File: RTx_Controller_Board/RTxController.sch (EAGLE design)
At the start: 91 parts, among them IC1 LTC4263, IC2 TLK110", U2 TPD4S012, X4 MINI-USB-32005-301

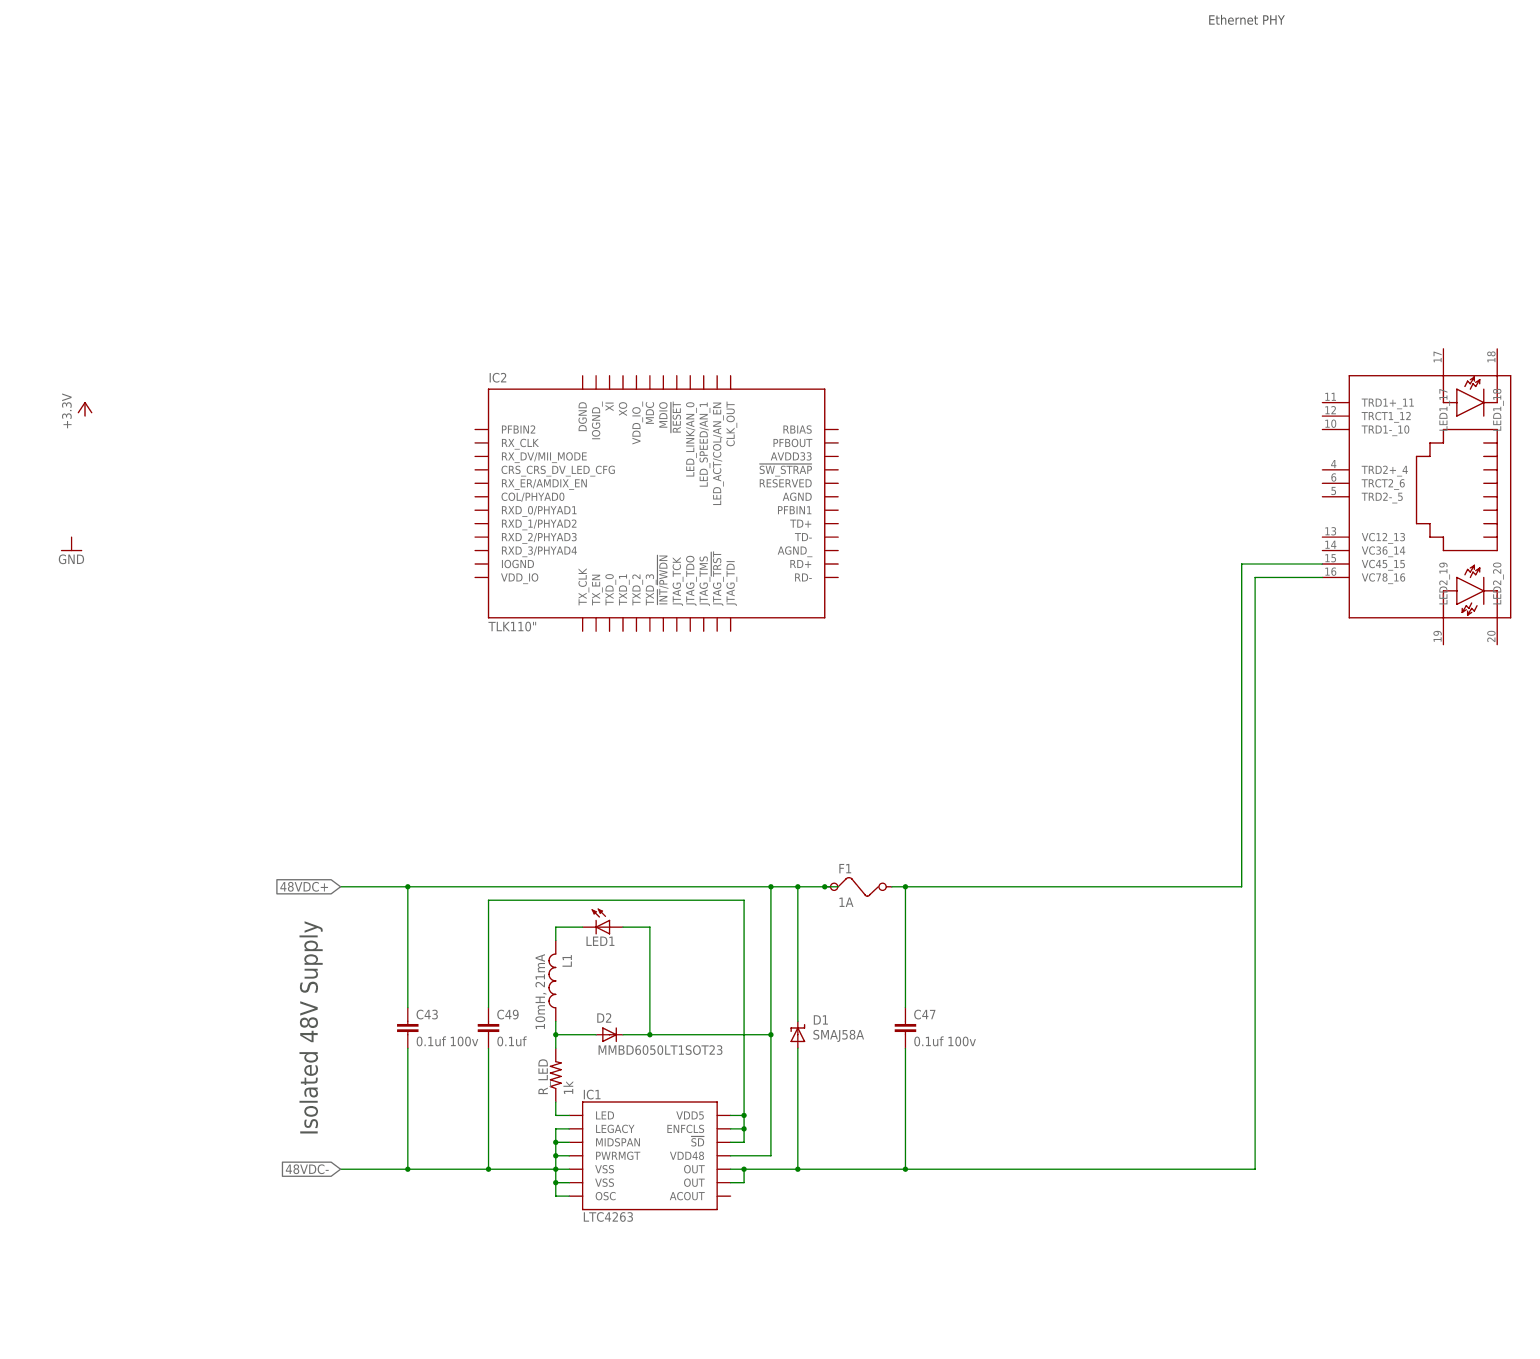
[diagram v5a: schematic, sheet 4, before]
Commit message: Updated Ethernet PHY components and schematic.
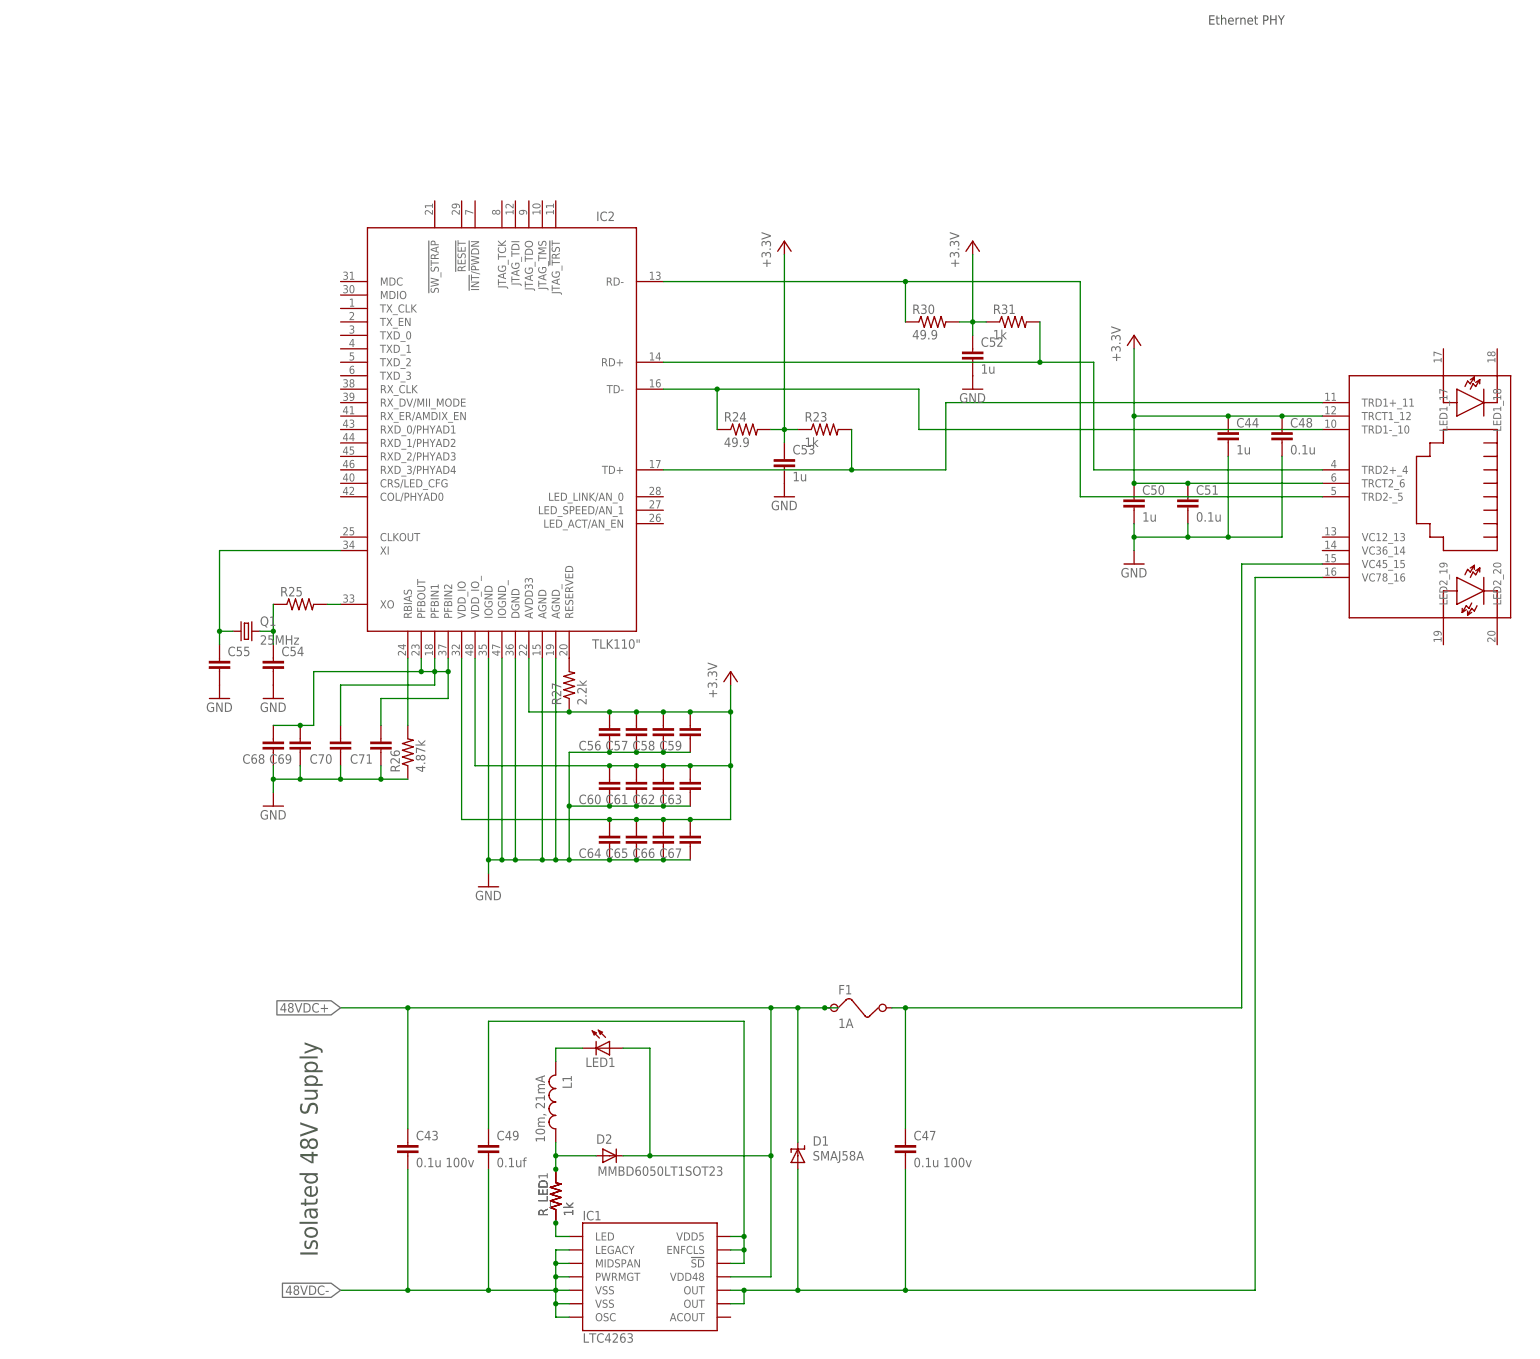
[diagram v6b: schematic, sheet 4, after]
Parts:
- added C44, C50, C52, C53: 1u, motorFeedback:C-EUC0805K
- added C48, C51: 0.1u, motorFeedback:C-EUC0805K
- added C54, C55, C56, C57, C58, C59, C60, C61, C62, C63, C64, C65, C66, C67, C68, C69, C70, C71: (no value), motorFeedback:C-EUC0805K
- added Q1: 25MHz, motorFeedback:CRYTAL
- added R23, R31, R_LED1: 1k, motorFeedback:R-US_R0603
- added R24, R30: 49.9, motorFeedback:R-US_R0603
- added R25: (no value), motorFeedback:R-US_R0603
- added R26: 4.87k, motorFeedback:R-US_R0603
- added R27: 2.2k, motorFeedback:R-US_R0603
- C43, C47: value 0.1uf 100v -> 0.1u 100v
- L1: value 10mH, 21mA -> 10m, 21mA
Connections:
- new net N$26: IC2.TD+, R23.2, U$6.TRD1+_11
- new net N$27: IC2.TD-, R24.1, U$6.TRD1-_10
- new net N$28: IC2.RD+, R31.2, U$6.TRD2+_4
- new net N$29: IC2.RD-, R30.1, U$6.TRD2-_5
- new net N$30: C53.1, R23.1, R24.2
- new net N$31: IC2.XO, R25.2
- new net N$32: C55.1, IC2.XI, Q1.1
- new net N$33: C54.1, Q1.2, R25.1
- new net N$34: IC2.RESERVED, R27.2
- new net N$40: IC2.RBIAS, R26.2
- new net N$41: C68.2, C69.2, C70.2, C71.2, IC2.PFBIN1, IC2.PFBIN2, IC2.PFBOUT
- net +3.3V: now also C44.1, C48.1, C50.1, C51.1, C52.1, C56.2, C57.2, C58.2, C59.2, C60.2, C61.2, C62.2, C63.2, C64.2, C65.2, C66.2, C67.2, IC2.AVDD33, IC2.VDD_IO, IC2.VDD_IO_, R27.1, R30.2, R31.1, U$6.TRCT1_12, U$6.TRCT2_6
- net GND: now also C44.2, C48.2, C50.2, C51.2, C52.2, C53.2, C54.2, C55.2, C56.1, C57.1, C58.1, C59.1, C60.1, C61.1, C62.1, C63.1, C64.1, C65.1, C66.1, C67.1, C68.1, C69.1, C70.1, C71.1, IC2.AGND, IC2.AGND_, IC2.DGND, IC2.IOGND, IC2.IOGND_, R26.1
- net N$24: now also R_LED1.2
- net N$25: now also R_LED1.1
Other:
- moved on the sheet: C43, C47, C49, D1, D2, F1, IC1, L1, LED1, R_LED

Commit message: Added Ethernet pinouts to MCU.
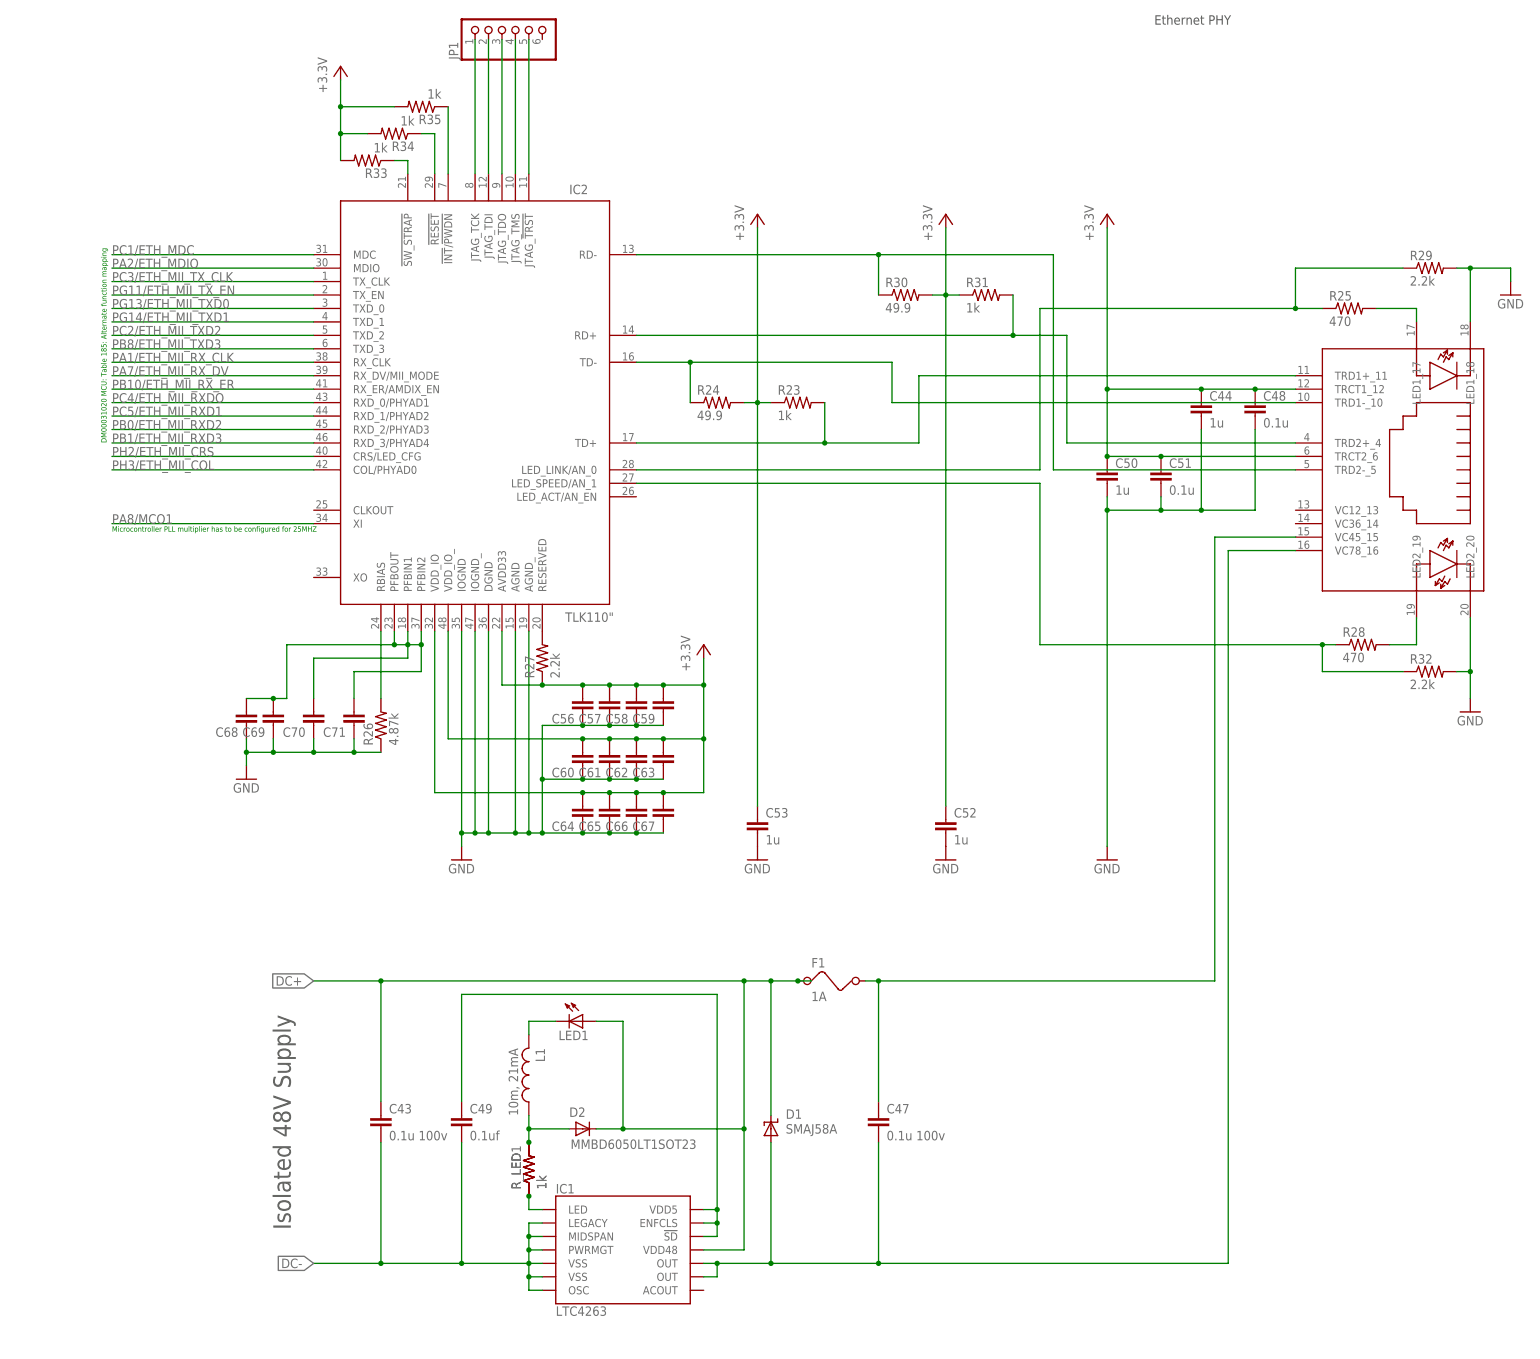
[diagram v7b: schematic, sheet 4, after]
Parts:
- removed C54, C55: (no value), motorFeedback:C-EUC0805K
- removed Q1: 25MHz, motorFeedback:CRYTAL
- added JP1: (no value), motorFeedback:PINHD-1X6
- added R28: 470, motorFeedback:R-US_R0603
- added R29, R32: 2.2k, motorFeedback:R-US_R0603
- added R33, R34, R35: 1k, motorFeedback:R-US_R0603
- R25: value (none) -> 470
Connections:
- net 48VDC+ renamed DC+
- net 48VDC- renamed DC-
- new net N$35: R25.2, U$6.LED1_17
- new net N$36: IC2.LED_SPEED/AN_1, R28.1, R32.1
- new net N$37: IC2.!RESET!, R34.1
- new net N$38: IC2.!INT!/!PWDN!, R35.1
- new net N$56: IC2.JTAG_TCK, JP1.1
- new net N$57: IC2.JTAG_TDI, JP1.2
- new net N$58: IC2.JTAG_TDO, JP1.3
- new net N$59: IC2.JTAG_TMS, JP1.4
- new net N$60: IC2.JTAG_!TRST!, JP1.5
- new net PA1/ETH_MII_RX_CLK: IC2.RX_CLK
- new net PA2/ETH_MDIO: IC2.MDIO
- new net PA7/ETH_MII_RX_DV: IC2.RX_DV/MII_MODE
- new net PA8/MCO1: IC2.XI
- new net PB0/ETH_MII_RXD2: IC2.RXD_2/PHYAD3
- new net PB1/ETH_MII_RXD3: IC2.RXD_3/PHYAD4
- new net PB10/ETH_MII_RX_ER: IC2.RX_ER/AMDIX_EN
- new net PB8/ETH_MII_TXD3: IC2.TXD_3
- new net PC1/ETH_MDC: IC2.MDC
- new net PC2/ETH_MII_TXD2: IC2.TXD_2
- new net PC3/ETH_MII_TX_CLK: IC2.TX_CLK
- new net PC4/ETH_MII_RXDO: IC2.RXD_0/PHYAD1
- new net PC5/ETH_MII_RXD1: IC2.RXD_1/PHYAD2
- new net PG11/ETH_MII_TX_EN: IC2.TX_EN
- new net PG13/ETH_MII_TXD0: IC2.TXD_0
- new net PG14/ETH_MII_TXD1: IC2.TXD_1
- new net PH2/ETH_MII_CRS: IC2.CRS/LED_CFG
- new net PH3/ETH_MII_COL: IC2.COL/PHYAD0
- net +3.3V: now also R33.2, R34.2, R35.2
- net GND: now also R29.2, R32.2, U$6.LED1_18, U$6.LED2_20; no longer C54.2, C55.2
- net N$31: now also IC2.!SW_STRAP!, R33.1; no longer IC2.XO, R25.2
- net N$32: now also R28.2, U$6.LED2_19; no longer C55.1, IC2.XI, Q1.1
- net N$33: now also IC2.LED_LINK/AN_0, R29.1; no longer C54.1, Q1.2
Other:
- note added: "DM00031020 MCU: Table 185: Alternate function mapping"
- note added: "Microcontroller PLL multiplier has to be configured for 25MHZ"
- moved on the sheet: C43, C44, C47, C48, C49, C50, C51, C52, C53, C56, C57, C58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

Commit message: Added CPU to schematic, completed pin-out of GMD signals, Ethernet signals, USB signals. Needs JTAG connector, ESD protection.
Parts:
- added C100, C101, C102, C103, C104, C105, C106, C107, C108, C109, C110, C111, C112, C113, C114, C115, C116, C117, C118, C119, C120, C121, C122, C123, C124, C93, C94, C95, C96, C97, C98, C99: (no value), motorFeedback:C-EUC0603
- added C54, C55, C72, C73, C74, C75, C76, C77, C78, C79, C80, C81, C82, C83, C84, C88, C90, C92: 0.1u, motorFeedback:C-EUC0402
- added C85: 4.7u, motorFeedback:C-EUC0603
- added C86, C87: 2.2u, motorFeedback:C-EUC0402
- added C89, C91: 1.0u, motorFeedback:C-EUC0402
- added R36: 0, motorFeedback:R-US_R0603
- added R37, R39, R40, R41, R42, R43, R44, R45, R46, R47, R48, R49, R50, R51, R52, R53: (no value), motorFeedback:R-US_R0603
- added R38: 10k, motorFeedback:R-US_R0603
- added SW1: COM08720, motorFeedback:COM08720
- added U1: STM32F407ZXT, motorFeedback:STM32F407ZXT
- added X3: (no value), con-subd:F15HDHS
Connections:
- removed net CNV: ADC1.CNV@6, ADC1.SDI@9, ADC2.CNV@6, ADC3.CNV@6, ADC4.CNV@6
- removed net PA1/ETH_MII_RX_CLK: IC2.RX_CLK
- removed net PA10/ID: U2.ID, X4.4
- removed net PA11/D-: R21.2
- removed net PA12/D+: R22.2
- removed net PA2/ETH_MDIO: IC2.MDIO
- removed net PA7/ETH_MII_RX_DV: IC2.RX_DV/MII_MODE
- removed net PA8/MCO1: IC2.XI
- removed net PA9/BBUS: C45.1, C46.1, U2.VBUS, X4.1
- removed net PB0/ETH_MII_RXD2: IC2.RXD_2/PHYAD3
- removed net PB1/ETH_MII_RXD3: IC2.RXD_3/PHYAD4
- removed net PB10/ETH_MII_RX_ER: IC2.RX_ER/AMDIX_EN
- removed net PB8/ETH_MII_TXD3: IC2.TXD_3
- removed net PC1/ETH_MDC: IC2.MDC
- removed net PC2/ETH_MII_TXD2: IC2.TXD_2
- removed net PC3/ETH_MII_TX_CLK: IC2.TX_CLK
- removed net PC4/ETH_MII_RXDO: IC2.RXD_0/PHYAD1
- removed net PC5/ETH_MII_RXD1: IC2.RXD_1/PHYAD2
- removed net PG11/ETH_MII_TX_EN: IC2.TX_EN
- removed net PG13/ETH_MII_TXD0: IC2.TXD_0
- removed net PG14/ETH_MII_TXD1: IC2.TXD_1
- removed net PH2/ETH_MII_CRS: IC2.CRS/LED_CFG
- removed net PH3/ETH_MII_COL: IC2.COL/PHYAD0
- removed net SCK: ADC1.SCK@8, ADC2.SCK@8, ADC3.SCK@8, ADC4.SCK@8
- removed net SDO: R16.2, R20.2
- new net ENABLE_AXIS3_OUT: C116.1, R46.2, U1-IO.PD0@81
- new net ENABLE_AXIS4_OUT: C114.1, R48.2, U1-IO.PD2@83
- new net ENABLE_LAT_OUT: C107.1, R43.2, U1-IO.PD11@58
- new net ENABLE_VERT_OUT: C105.1, R45.2, U1-IO.PD6@87
- new net ETH_MCO1: IC2.XI, U1-IO.PA8/MCO1@67
- new net ETH_MDC: IC2.MDC, U1-IO.PC1/ETH_MDC@16
- new net ETH_MDIO: IC2.MDIO, U1-IO.PA2/ETH_MDIO@25
- new net ETH_MII_COL: IC2.COL/PHYAD0, U1-IO.PA3/ETH_MII_COL@26
- new net ETH_MII_CRS: IC2.CRS/LED_CFG, U1-IO.PA0/ETH_MII_CRS@23
- new net ETH_MII_RXD0: IC2.RXD_0/PHYAD1, U1-IO.PC4/ETH_MII_RXD0@33
- new net ETH_MII_RXD1: IC2.RXD_1/PHYAD2, U1-IO.PC5/ETH_MII_RXD1@34
- new net ETH_MII_RXD2: IC2.RXD_2/PHYAD3, U1-IO.PB0/ETH_MII_RXD2@35
- new net ETH_MII_RXD3: IC2.RXD_3/PHYAD4, U1-IO.PB1/ETH_MII_RXD3@36
- new net ETH_MII_RX_CLK: IC2.RX_CLK, U1-IO.PA1/ETH_MII_RX_CLK@24
- new net ETH_MII_RX_DV: IC2.RX_DV/MII_MODE, U1-IO.PA7/ETH_MII_RX_DV@32
- new net ETH_MII_RX_ER: IC2.RX_ER/AMDIX_EN, U1-IO.PB10/ETH_MII_RX_ER@47
- new net ETH_MII_TXD0: IC2.TXD_0, U1-IO.PB12/ETH_MII_TXD0@51
- new net ETH_MII_TXD1: IC2.TXD_1, U1-IO.PB13/ETH_MII_TXD1@52
- new net ETH_MII_TXD2: IC2.TXD_2, U1-IO.PC2/ETH_MII_TXD2@17
- new net ETH_MII_TXD3: IC2.TXD_3, U1-IO.PB8/ETH_MII_TXD3@95
- new net ETH_MII_TX_CLK: IC2.TX_CLK, U1-IO.PC3/ETH_MII_TX_CLK@18
- new net ETH_MII_TX_EN: IC2.TX_EN, U1-IO.PB11/ETH_MII_TX_EN@48
- new net N$39: C92.1, SW1.1@1, SW1.3@3, U1-PWR.NRST@14
- new net N$42: C96.1, R37.1, X2-15.F
- new net N$43: R36.2, U1-PWR.VBAT@6
- new net N$44: R38.1, U1-PWR.BOOT0@94
- new net N$45: C95.1, R39.1, X2-14.F
- new net N$46: C94.1, R40.1, X2-13.F
- new net N$47: C93.1, R41.1, X2-12.F
- new net N$48: C104.1, R42.1, X2-4.F
- new net N$49: C103.1, R43.1, X2-3.F
- new net N$50: C102.1, R44.1, X2-2.F
- new net N$51: C101.1, R45.1, X2-1.F
- new net N$52: C112.1, R46.1, X3-4.F
- new net N$53: C111.1, R47.1, X3-3.F
- new net N$54: C110.1, R48.1, X3-2.F
- new net N$55: C109.1, R49.1, X3-1.F
- new net N$61: C120.1, R50.1, X3-15.F
- new net N$62: C119.1, R51.1, X3-14.F
- new net N$63: C118.1, R52.1, X3-13.F
- new net N$64: C117.1, R53.1, X3-12.F
- new net PWM_AXIS3_U_OUT: C123.1, R51.2, U1-IO.PC7@64
- new net PWM_AXIS3_V_OUT: C124.1, R50.2, U1-IO.PC6@63
- new net PWM_AXIS4_U_OUT: C121.1, R53.2, U1-IO.PC9@66
- new net PWM_AXIS4_V_OUT: C122.1, R52.2, U1-IO.PC8@65
- new net PWM_LAT_U_OUT: C97.1, R41.2, U1-IO.PD15@62
- new net PWM_LAT_V_OUT: C98.1, R40.2, U1-IO.PD14@61
- new net PWM_VERT_U_OUT: C99.1, R39.2, U1-IO.PD13@60
- new net PWM_VERT_V_OUT: C100.1, R37.2, U1-IO.PD12@59
- new net SPI_MISO: R16.2, R20.2, U1-IO.PA6/SPI_MISO@31
- new net SPI_MOSI: ADC1.CNV@6, ADC1.SDI@9, ADC2.CNV@6, ADC3.CNV@6, ADC4.CNV@6, U1-IO.PB5/SPI1_MOSI@91
- new net SPI_NCS: U1-IO.PA4/SPI_NSS@29
- new net SPI_SCK: ADC1.SCK@8, ADC2.SCK@8, ADC3.SCK@8, ADC4.SCK@8, U1-IO.PA5/SPI_SCK@30
- new net USB_D+: R22.2, U1-IO.PA12/OTG_FS_DP@71
- new net USB_D-: R21.2, U1-IO.PA11/OTG_FS_DM@70
- new net USB_ID: U1-IO.PA10/OTG_FS_ID@69, U2.ID, X4.4
- new net USB_VBUS: C45.1, C46.1, U1-IO.PA9/OTG_FS_VBUS@68, U2.VBUS, X4.1
- new net VCAP_1@49: C87.1, U1-PWR.VCAP_1@49
- new net VCAP_2@73: C86.1, U1-PWR.VCAP_2@73
- new net VDDA@22: C88.1, C89.1, C90.1, C91.1, U1-PWR.VDDA@22, U1-PWR.VREF+@21
- new net WATCHDOG_AXIS3_OUT: C115.1, R47.2, U1-IO.PD1@82
- new net WATCHDOG_AXIS4_OUT: C113.1, R49.2, U1-IO.PD3@84
- new net WATCHDOG_LAT_OUT: C108.1, R42.2, U1-IO.PD10@57
- new net WATCHDOG_VERT_OUT: C106.1, R44.2, U1-IO.PD5@86
- net +3.3V: now also C54.1, C55.1, C72.1, C73.1, C74.1, C75.1, C76.1, C77.1, C78.1, C79.1, C80.1, C81.1, C82.1, C83.1, C84.1, C85.1, R36.1, U1-PWR.VDD@100, U1-PWR.VDD@11, U1-PWR.VDD@19, U1-PWR.VDD@28, U1-PWR.VDD@50, U1-PWR.VDD@75
- net GND: now also C100.2, C101.2, C102.2, C103.2, C104.2, C105.2, C106.2, C107.2, C108.2, C109.2, C110.2, C111.2, C112.2, C113.2, C114.2, C115.2, C116.2, C117.2, C118.2, C119.2, C120.2, C121.2, C122.2, C123.2, C124.2, C54.2, C55.2, C72.2, C73.2, C74.2, C75.2, C76.2, C77.2, C78.2, C79.2, C80.2, C81.2, C82.2, C83.2, C84.2, C85.2, C86.2, C87.2, C88.2, C89.2, C90.2, C91.2, C92.2, C93.2, C94.2, C95.2, C96.2, C97.2, C98.2, C99.2, JP1.6, R38.2, SW1.2@2, SW1.4@4, U1-PWR.VSS@10, U1-PWR.VSS@27, U1-PWR.VSS@74, U1-PWR.VSS@99, U1-PWR.VSSA@20, X2-10.F, X2-5.F, X2-6.F, X2-7.F, X2-8.F, X3-10.F, X3-5.F, X3-6.F, X3-7.F, X3-8.F
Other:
- note added: "HW RESET"
- moved on the sheet: C45, C46, R21, R22, U2, X2-1, X2-10, X2-11, X2-12, X2-13, X2-14, X2-15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
